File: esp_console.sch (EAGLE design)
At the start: 41 parts, among them IC1 74AHC1G04DBV, IC2 UA78M05DCY, J2 10118193-0001LF, Q1 12mhz, Q2 ON_SEMICONDUCTOR_BC849BLT1GON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, Q3 ON_SEMICONDUCTOR_BC849BLT1GON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, SW1 OS102011MA1Q, U3 74HC4051D

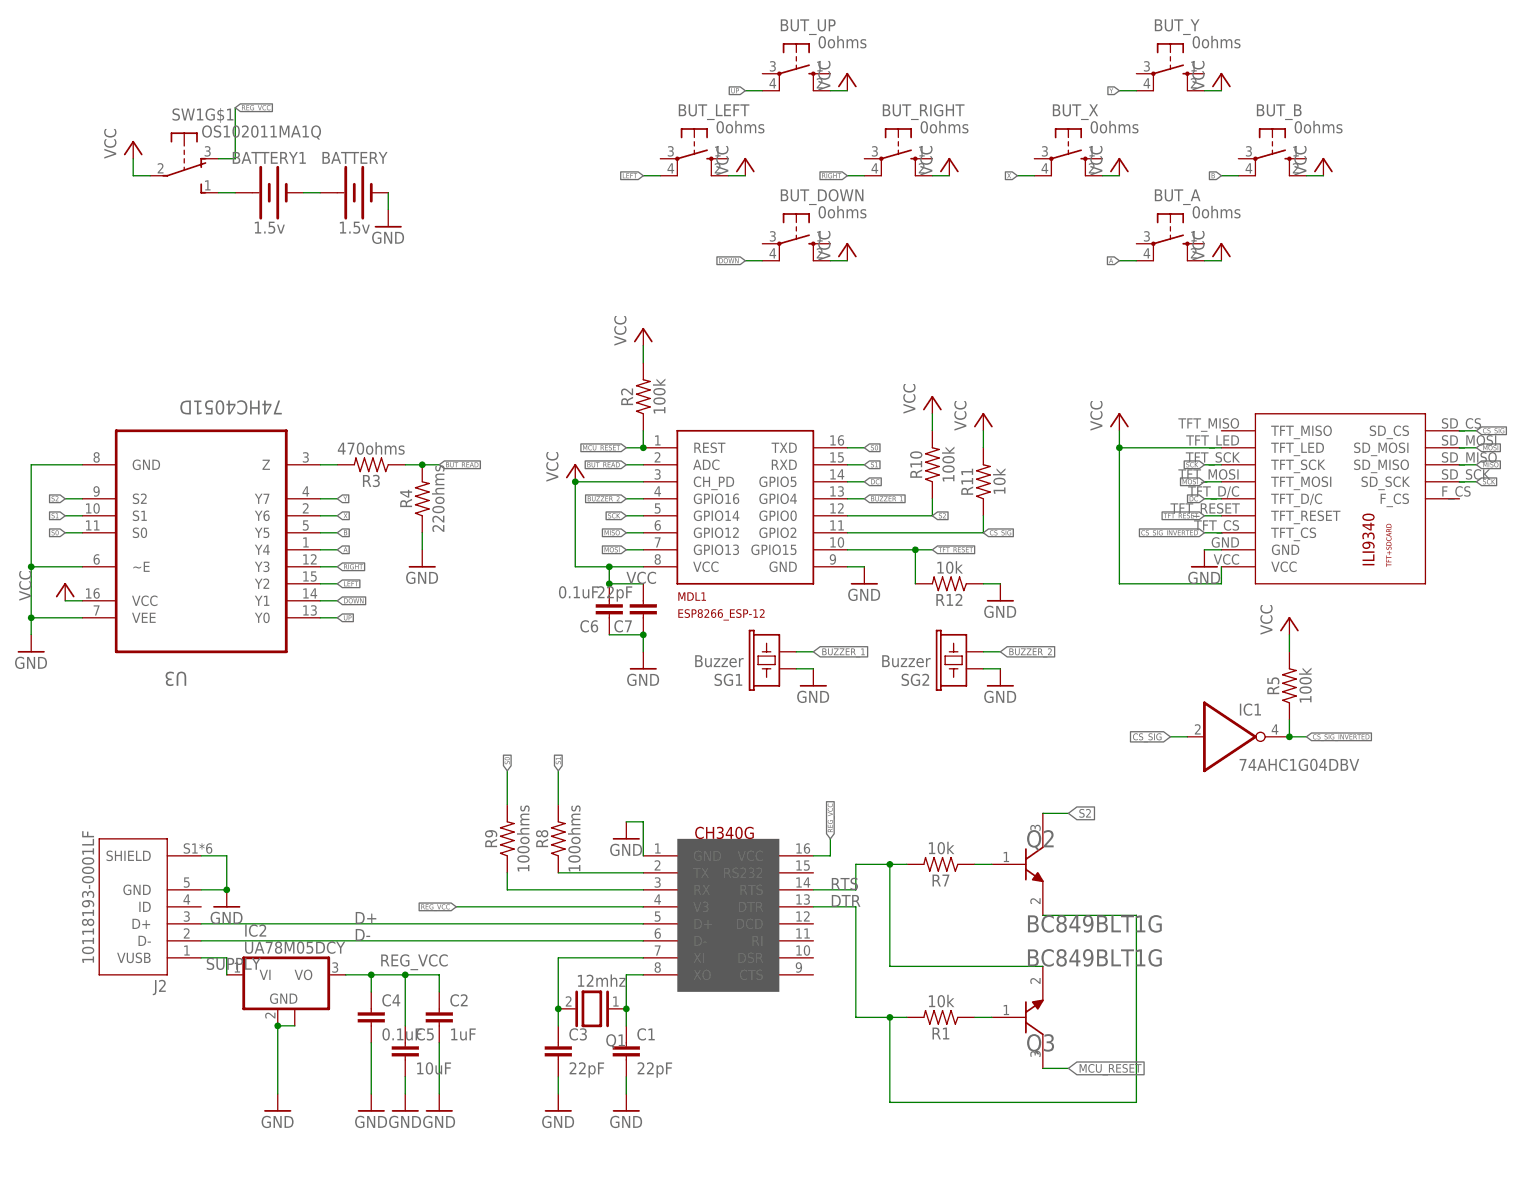
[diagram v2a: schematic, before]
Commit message: Slight revision to wire routing, new gerbers
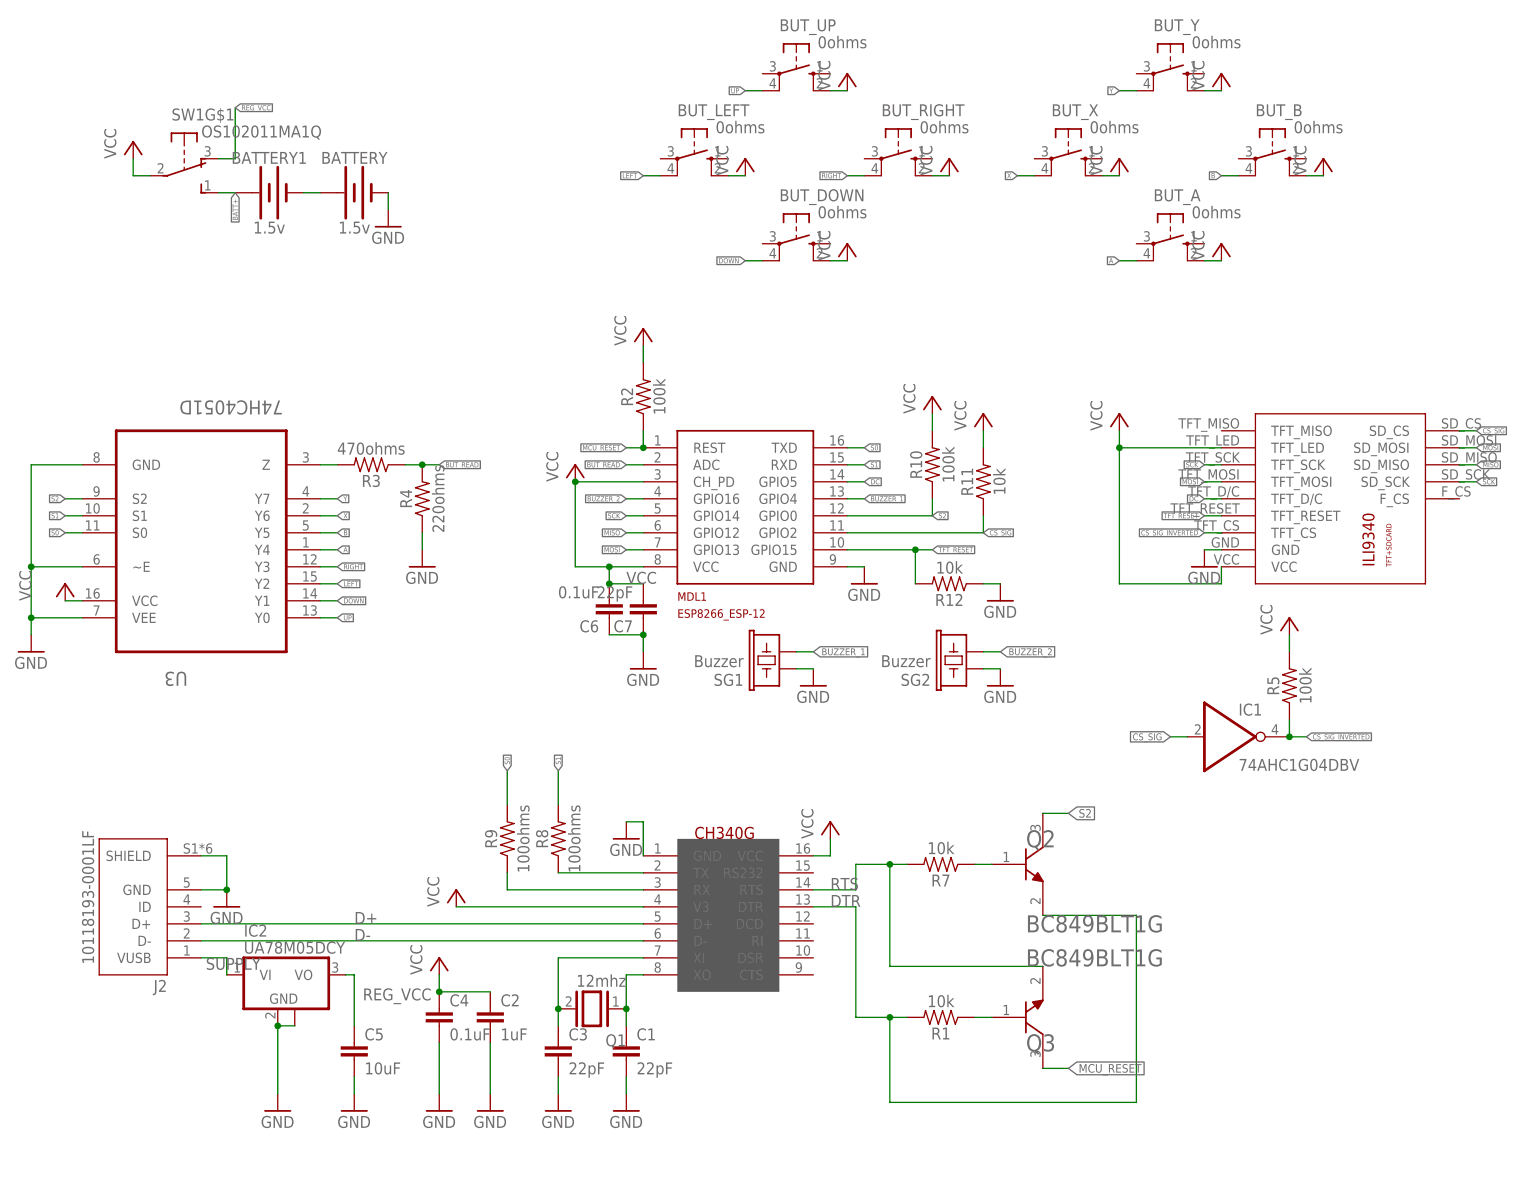
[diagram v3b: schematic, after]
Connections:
- net REG_VCC: no longer C2.1, C4.1, U$1.V3, U$1.VCC
- net VCC: now also C2.1, C4.1, U$1.V3, U$1.VCC
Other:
- moved on the sheet: C2, C4, C5
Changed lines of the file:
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@@
 <part name="R5" library="SparkFun-Resistors" library_urn="urn:adsk.eagle:library:532" deviceset="10KOHM" device="-0603-1/10W-1%" package3d_urn="urn:adsk.eagle:package:39650/1" value="100k"/>
 <part name="P+1" library="supply1" library_urn="urn:adsk.eagle:library:371" deviceset="VCC" device=""/>
+<part name="P+2" library="supply1" library_urn="urn:adsk.eagle:library:371" deviceset="VCC" device=""/>
+<part name="P+8" library="supply1" library_urn="urn:adsk.eagle:library:371" deviceset="VCC" device=""/>
+<part name="P+19" library="supply1" library_urn="urn:adsk.eagle:library:371" deviceset="VCC" device=""/>
 </parts>
 <sheets>
@@
 <attribute name="VALUE" x="-55.88" y="-76.2" size="1.778" layer="96"/>
 </instance>
-<instance part="C4" gate="G$1" x="-91.44" y="-99.06" smashed="yes">
-<attribute name="NAME" x="-89.916" y="-98.679" size="1.778" layer="95"/>
-<attribute name="VALUE" x="-89.916" y="-103.759" size="1.778" layer="96"/>
-</instance>
-<instance part="C5" gate="G$1" x="-86.36" y="-104.14" smashed="yes">
-<attribute name="NAME" x="-84.836" y="-103.759" size="1.778" layer="95"/>
-<attribute name="VALUE" x="-84.836" y="-108.839" size="1.778" layer="96"/>
-</instance>
-<instance part="GND18" gate="1" x="-91.44" y="-114.3" smashed="yes">
-<attribute name="VALUE" x="-93.98" y="-116.84" size="1.778" layer="96"/>
-</instance>
-<instance part="GND" gate="1" x="-86.36" y="-114.3" smashed="yes">
-<attribute name="VALUE" x="-88.9" y="-116.84" size="1.778" layer="96"/>
-</instance>
-<instance part="GND20" gate="1" x="-81.28" y="-114.3" smashed="yes">
+<instance part="C4" gate="G$1" x="-81.28" y="-99.06" smashed="yes">
+<attribute name="NAME" x="-79.756" y="-98.679" size="1.778" layer="95"/>
+<attribute name="VALUE" x="-79.756" y="-103.759" size="1.778" layer="96"/>
+</instance>
+<instance part="C5" gate="G$1" x="-93.98" y="-104.14" smashed="yes">
+<attribute name="NAME" x="-92.456" y="-103.759" size="1.778" layer="95"/>
+<attribute name="VALUE" x="-92.456" y="-108.839" size="1.778" layer="96"/>
+</instance>
+<instance part="GND18" gate="1" x="-81.28" y="-114.3" smashed="yes">
 <attribute name="VALUE" x="-83.82" y="-116.84" size="1.778" layer="96"/>
+</instance>
+<instance part="GND" gate="1" x="-93.98" y="-114.3" smashed="yes">
+<attribute name="VALUE" x="-96.52" y="-116.84" size="1.778" layer="96"/>
+</instance>
+<instance part="GND20" gate="1" x="-73.66" y="-114.3" smashed="yes">
+<attribute name="VALUE" x="-76.2" y="-116.84" size="1.778" layer="96"/>
 </instance>
 <instance part="J2" gate="G$1" x="-127" y="-83.82" smashed="yes" rot="R180">
@@
 <attribute name="VALUE" x="-142.24" y="-38.1" size="1.778" layer="96" rot="R90"/>
 </instance>
-<instance part="C2" gate="G$1" x="-81.28" y="-99.06" smashed="yes">
-<attribute name="NAME" x="-79.756" y="-98.679" size="1.778" layer="95"/>
-<attribute name="VALUE" x="-79.756" y="-103.759" size="1.778" layer="96"/>
+<instance part="C2" gate="G$1" x="-73.66" y="-99.06" smashed="yes">
+<attribute name="NAME" x="-72.136" y="-98.679" size="1.778" layer="95"/>
+<attribute name="VALUE" x="-72.136" y="-103.759" size="1.778" layer="96"/>
 </instance>
 <instance part="R5" gate="G$1" x="45.72" y="-50.8" smashed="yes" rot="R90">
@@
 <instance part="P+1" gate="VCC" x="45.72" y="-40.64" smashed="yes">
 <attribute name="VALUE" x="43.18" y="-43.18" size="1.778" layer="96" rot="R90"/>
+</instance>
+<instance part="P+2" gate="VCC" x="-78.74" y="-81.28" smashed="yes">
+<attribute name="VALUE" x="-81.28" y="-83.82" size="1.778" layer="96" rot="R90"/>
+</instance>
+<instance part="P+8" gate="VCC" x="-22.86" y="-71.12" smashed="yes">
+<attribute name="VALUE" x="-25.4" y="-73.66" size="1.778" layer="96" rot="R90"/>
+</instance>
+<instance part="P+19" gate="VCC" x="-81.28" y="-91.44" smashed="yes">
+<attribute name="VALUE" x="-83.82" y="-93.98" size="1.778" layer="96" rot="R90"/>
 </instance>
 </instances>
@@
 <pinref part="P+1" gate="VCC" pin="VCC"/>
 </segment>
+<segment>
+<pinref part="U$1" gate="G$1" pin="VCC"/>
+<wire x1="-25.4" y1="-76.2" x2="-22.86" y2="-76.2" width="0.1524" layer="91"/>
+<wire x1="-22.86" y1="-76.2" x2="-22.86" y2="-73.66" width="0.1524" layer="91"/>
+<pinref part="P+8" gate="VCC" pin="VCC"/>
+</segment>
+<segment>
+<pinref part="U$1" gate="G$1" pin="V3"/>
+<wire x1="-50.8" y1="-83.82" x2="-78.74" y2="-83.82" width="0.1524" layer="91"/>
+<pinref part="P+2" gate="VCC" pin="VCC"/>
+</segment>
+<segment>
+<pinref part="C4" gate="G$1" pin="1"/>
+<pinref part="C2" gate="G$1" pin="1"/>
+<wire x1="-81.28" y1="-96.52" x2="-73.66" y2="-96.52" width="0.1524" layer="91"/>
+<pinref part="P+19" gate="VCC" pin="VCC"/>
+<wire x1="-81.28" y1="-93.98" x2="-81.28" y2="-96.52" width="0.1524" layer="91"/>
+<junction x="-81.28" y="-96.52"/>
+</segment>
 </net>
 <net name="MCU_RESET" class="0">
@@
 <pinref part="BATTERY1" gate="G$1" pin="+"/>
 <wire x1="-111.76" y1="22.86" x2="-114.3" y2="22.86" width="0.1524" layer="91"/>
+<label x="-111.76" y="22.86" size="0.762" layer="95" rot="R270" xref="yes"/>
 </segment>
 </net>
@@
 <segment>
 <pinref part="IC2" gate="G$1" pin="VO"/>
-<wire x1="-91.44" y1="-93.98" x2="-86.36" y2="-93.98" width="0.1524" layer="91"/>
-<pinref part="C4" gate="G$1" pin="1"/>
-<wire x1="-86.36" y1="-93.98" x2="-81.28" y2="-93.98" width="0.1524" layer="91"/>
-<wire x1="-91.44" y1="-96.52" x2="-91.44" y2="-93.98" width="0.1524" layer="91"/>
+<wire x1="-95.25" y1="-93.98" x2="-93.98" y2="-93.98" width="0.1524" layer="91"/>
 <pinref part="C5" gate="G$1" pin="1"/>
-<wire x1="-86.36" y1="-101.6" x2="-86.36" y2="-93.98" width="0.1524" layer="91"/>
-<junction x="-86.36" y="-93.98"/>
-<wire x1="-81.28" y1="-96.52" x2="-81.28" y2="-93.98" width="0.1524" layer="91"/>
-<label x="-90.17" y="-92.71" size="1.778" layer="95"/>
-<pinref part="C2" gate="G$1" pin="1"/>
-<wire x1="-95.25" y1="-93.98" x2="-91.44" y2="-93.98" width="0.1524" layer="91"/>
-<junction x="-91.44" y="-93.98"/>
+<wire x1="-93.98" y1="-101.6" x2="-93.98" y2="-93.98" width="0.1524" layer="91"/>
+<label x="-92.71" y="-97.79" size="1.778" layer="95"/>
 </segment>
 <segment>
@@
 <label x="-111.76" y="35.56" size="0.762" layer="95" xref="yes"/>
 <wire x1="-111.76" y1="27.94" x2="-111.76" y2="35.56" width="0.1524" layer="91"/>
-</segment>
-<segment>
-<pinref part="U$1" gate="G$1" pin="VCC"/>
-<wire x1="-25.4" y1="-76.2" x2="-22.86" y2="-76.2" width="0.1524" layer="91"/>
-<wire x1="-22.86" y1="-76.2" x2="-22.86" y2="-73.66" width="0.1524" layer="91"/>
-<label x="-22.86" y="-73.66" size="0.762" layer="95" rot="R90" xref="yes"/>
-</segment>
-<segment>
-<pinref part="U$1" gate="G$1" pin="V3"/>
-<wire x1="-50.8" y1="-83.82" x2="-78.74" y2="-83.82" width="0.1524" layer="91"/>
-<label x="-78.74" y="-83.82" size="0.762" layer="95" rot="R180" xref="yes"/>
 </segment>
 </net>
@@
 <pinref part="C4" gate="G$1" pin="2"/>
 <pinref part="GND18" gate="1" pin="GND"/>
-<wire x1="-91.44" y1="-104.14" x2="-91.44" y2="-111.76" width="0.1524" layer="91"/>
+<wire x1="-81.28" y1="-104.14" x2="-81.28" y2="-111.76" width="0.1524" layer="91"/>
 </segment>
 <segment>
 <pinref part="GND" gate="1" pin="GND"/>
 <pinref part="C5" gate="G$1" pin="2"/>
-<wire x1="-86.36" y1="-109.22" x2="-86.36" y2="-111.76" width="0.1524" layer="91"/>
+<wire x1="-93.98" y1="-109.22" x2="-93.98" y2="-111.76" width="0.1524" layer="91"/>
 </segment>
 <segment>
 <pinref part="GND20" gate="1" pin="GND"/>
-<wire x1="-81.28" y1="-111.76" x2="-81.28" y2="-104.14" width="0.1524" layer="91"/>
+<wire x1="-73.66" y1="-111.76" x2="-73.66" y2="-104.14" width="0.1524" layer="91"/>
 <pinref part="C2" gate="G$1" pin="2"/>
 </segment>
